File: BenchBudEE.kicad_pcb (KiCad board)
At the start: 4 copper layers, 165.1 x 63.5 mm, 0 parts

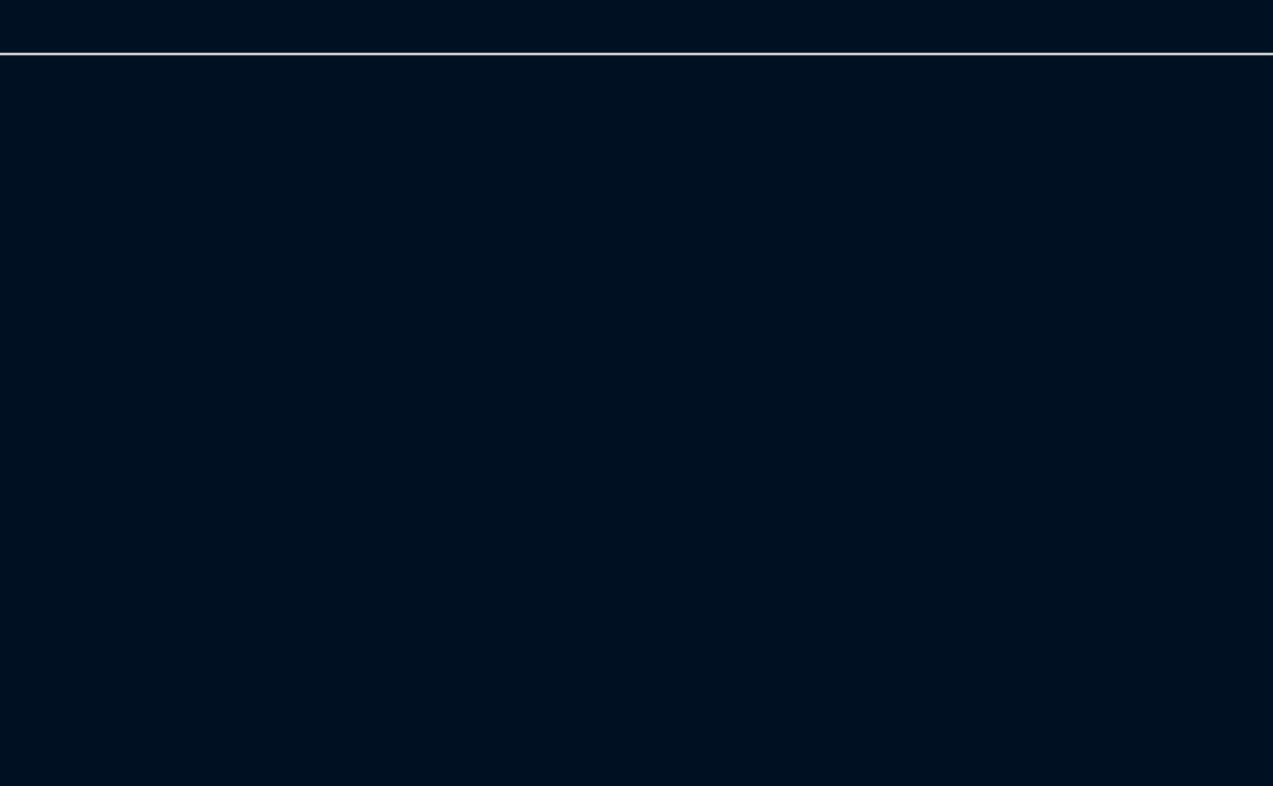
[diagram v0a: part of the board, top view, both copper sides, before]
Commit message: Relay module association and placement
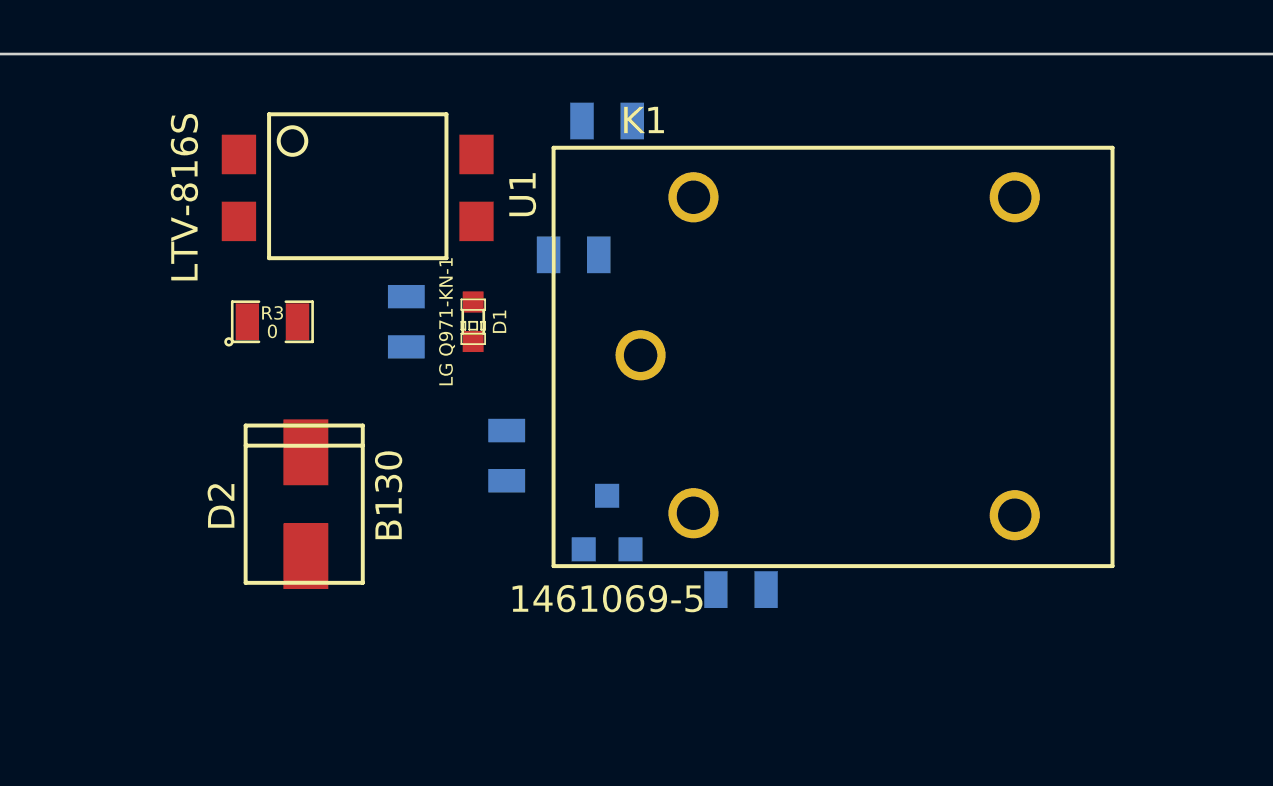
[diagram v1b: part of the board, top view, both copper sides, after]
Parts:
- added D1: LG Q971-KN-1, LED-0603, F.Cu at (251.5, 121.9)
- added D2: B130, SMA, F.Cu at (245.1, 130.8)
- added K1: 1461069-5, TE-SPDT, F.Cu at (257.8, 123.2)
- added Q1: 2N3904, SOT23EBC, B.Cu at (256.5, 129.5)
- added R1: 500, SM0805, B.Cu at (255.3, 119.4)
- added R2: 200, SM0805, B.Cu at (248.9, 121.9)
- added R3: 0, SM0805, F.Cu at (243.8, 121.9)
- added R4: 100, SM0805, B.Cu at (252.7, 127.0)
- added R5: 0, SM0805, B.Cu at (256.5, 114.3)
- added R6: 0, SM0805, B.Cu at (261.6, 132.1)
- added U1: LTV-816S, 4-SMD, F.Cu at (242.6, 115.6)

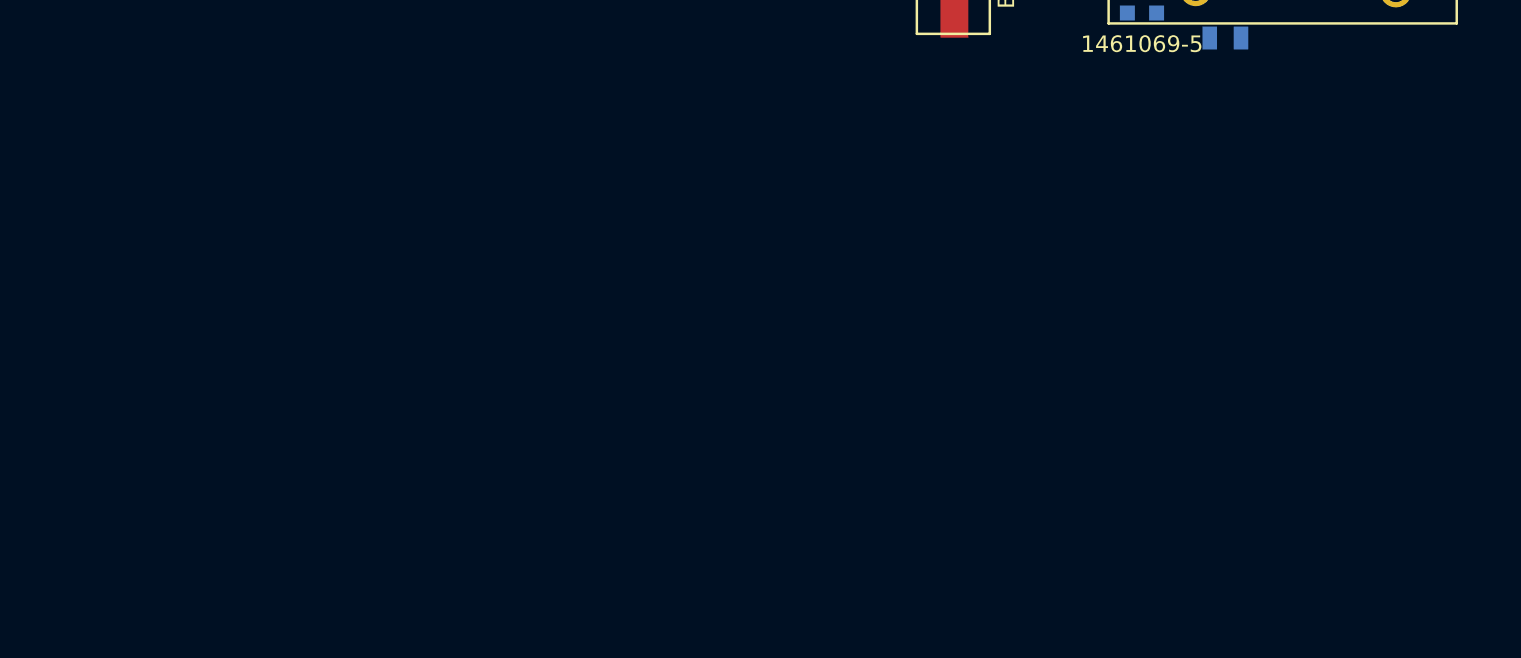
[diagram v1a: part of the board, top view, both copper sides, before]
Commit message: Thermocouple association and placement
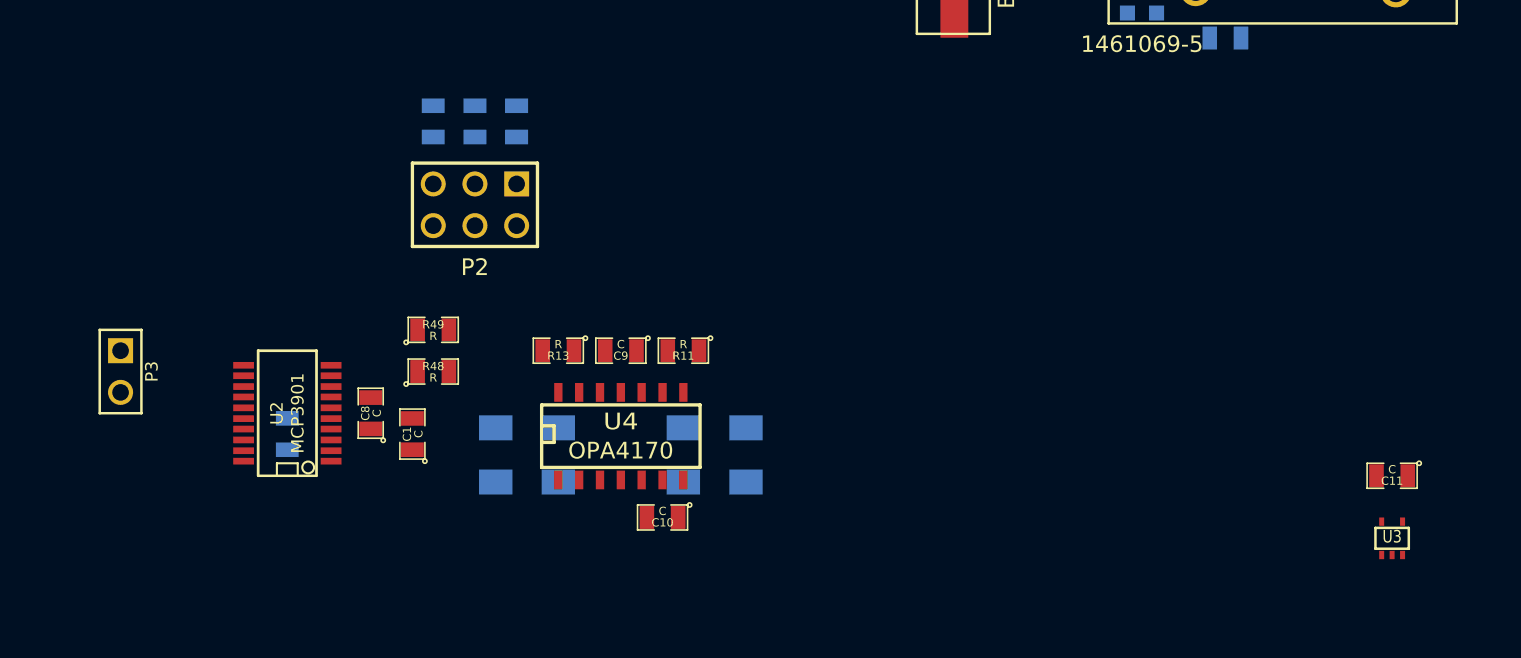
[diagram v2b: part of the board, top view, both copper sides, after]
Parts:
- added C1: C, SM0805, F.Cu at (212.1, 156.2)
- added C10: C, SM0805, F.Cu at (227.3, 161.3)
- added C11: C, SM0805, F.Cu at (271.8, 158.8)
- added C7: C, SM0805, B.Cu at (204.5, 156.2)
- added C8: C, SM0805, F.Cu at (209.6, 154.9)
- added C9: C, SM0805, F.Cu at (224.8, 151.1)
- added P2: CONN_3X2, pin_array_3x2, F.Cu at (215.9, 142.2)
- added P3: CONN_2, PIN_ARRAY_2X1, F.Cu at (194.3, 152.4)
- added R10: R, SM1206, B.Cu at (221.0, 157.5)
- added R11: R, SM0805, F.Cu at (228.6, 151.1)
- added R12: R, SM0805, B.Cu at (215.9, 137.2)
- added R13: R, SM0805, F.Cu at (221.0, 151.1)
- added R44: R, SM0805, B.Cu at (218.4, 137.2)
- added R45: R, SM0805, B.Cu at (213.4, 137.2)
- added R48: R, SM0805, F.Cu at (213.4, 152.4)
- added R49: R, SM0805, F.Cu at (213.4, 149.9)
- added R7: R, SM1206, B.Cu at (217.2, 157.5)
- added R8: R, SM1206, B.Cu at (228.6, 157.5)
- added R9: R, SM1206, B.Cu at (232.4, 157.5)
- added U2: MCP3901, SSOP20, F.Cu at (204.5, 154.9)
- added U3: LMT84, SOT353, F.Cu at (271.8, 162.6)
- added U4: OPA4170, SO14E, F.Cu at (224.8, 156.2)

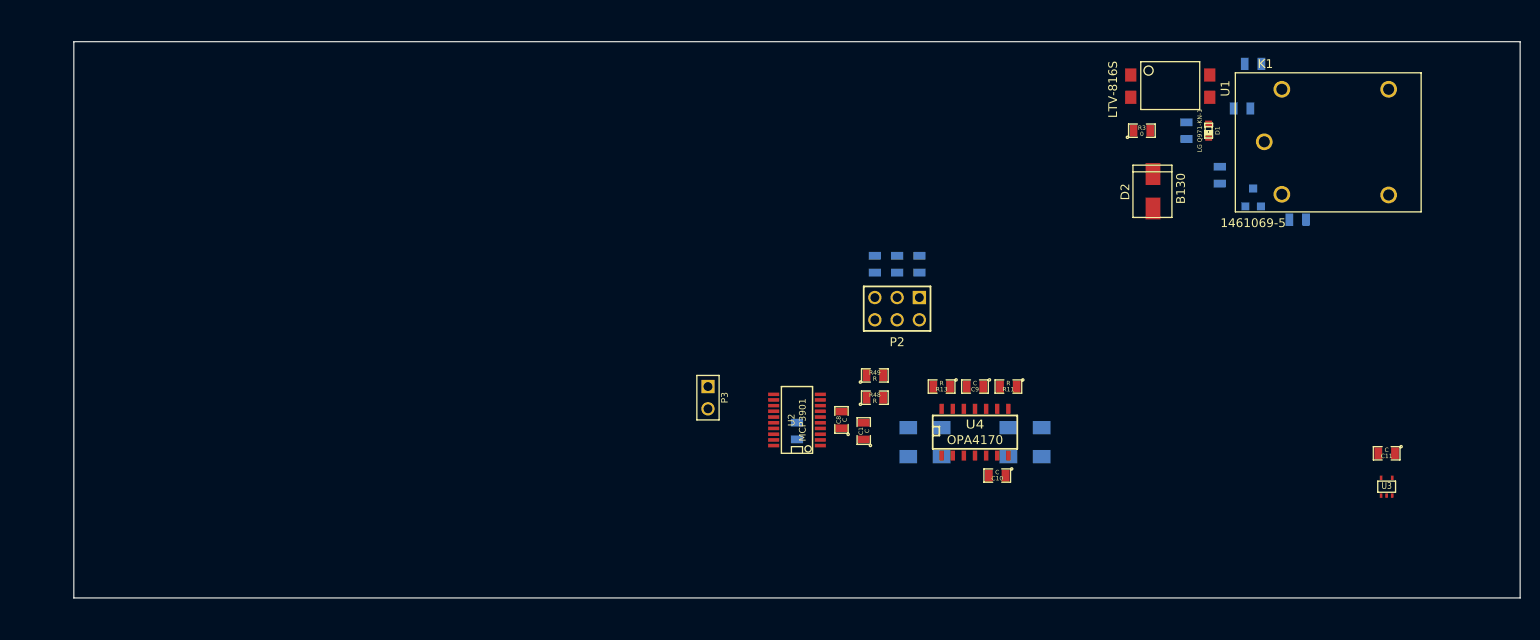
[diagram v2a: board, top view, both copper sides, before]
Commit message: Terminal block and Arduino: assc/placement
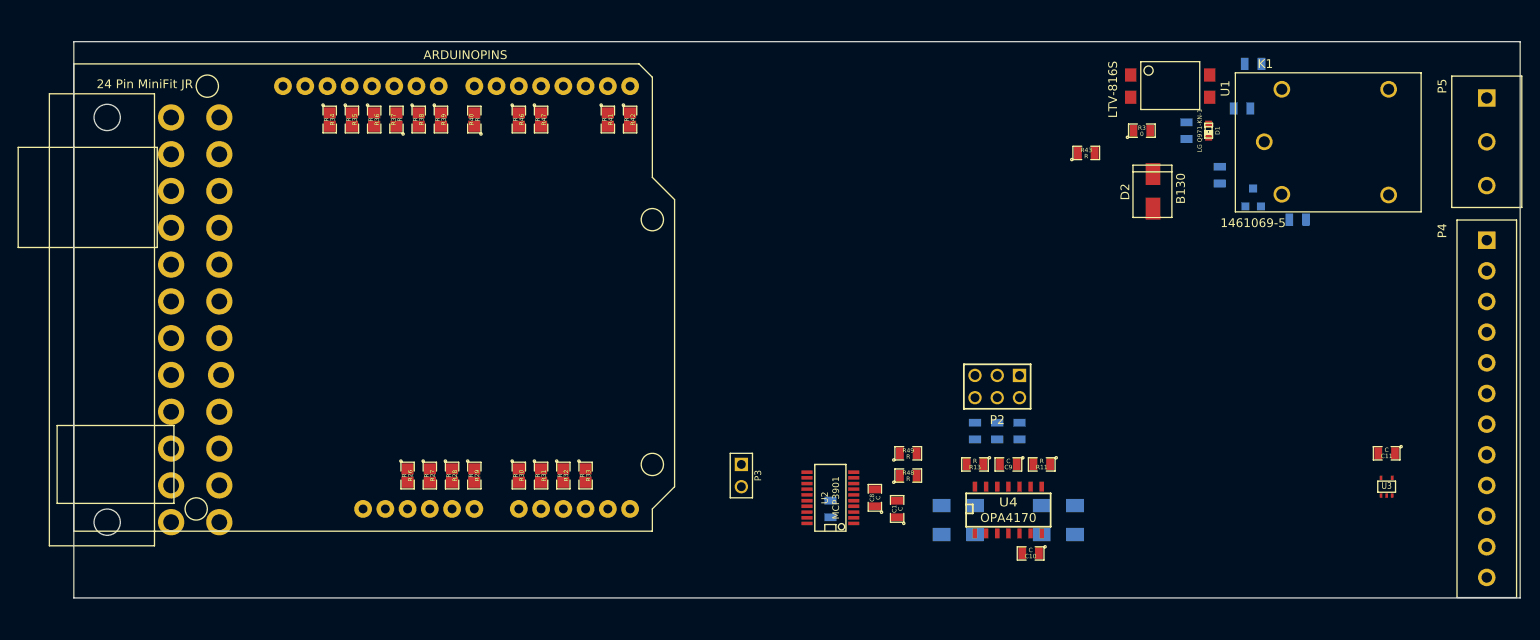
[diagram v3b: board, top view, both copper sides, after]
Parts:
- added ARD1: ARDUINOPINS, Arduino, F.Cu at (121.9, 167.6)
- added P1: 24 Pin MiniFit JR, ATXheader, F.Cu at (125.7, 143.5)
- added P4: 12 Pin Terminal Block, 12pinTB, F.Cu at (283.2, 153.7)
- added P5: 3 Pin TB, 3pinTB, F.Cu at (283.2, 123.2)
- added R26: R, SM0805-blob, F.Cu at (160.0, 161.3)
- added R27: R, SM0805-blob, F.Cu at (162.6, 161.3)
- added R28: R, SM0805-blob, F.Cu at (165.1, 161.3)
- added R29: R, SM0805-blob, F.Cu at (167.6, 161.3)
- added R30: R, SM0805-blob, F.Cu at (172.7, 161.3)
- added R31: R, SM0805-blob, F.Cu at (175.3, 161.3)
- added R32: R, SM0805-blob, F.Cu at (177.8, 161.3)
- added R33: R, SM0805-blob, F.Cu at (180.3, 161.3)
- added R34: R, SM0805-blob, F.Cu at (151.1, 120.7)
- added R35: R, SM0805-blob, F.Cu at (153.7, 120.7)
- added R36: R, SM0805-blob, F.Cu at (156.2, 120.7)
- added R37: R, SM0805-blob, F.Cu at (158.8, 120.7)
- added R38: R, SM0805-blob, F.Cu at (161.3, 120.7)
- added R39: R, SM0805-blob, F.Cu at (163.8, 120.7)
- added R40: R, SM0805-blob, F.Cu at (167.6, 120.7)
- added R41: R, SM0805-blob, F.Cu at (182.9, 120.7)
- added R42: R, SM0805-blob, F.Cu at (185.4, 120.7)
- added R43: R, SM0805, F.Cu at (237.5, 124.5)
- added R46: R, SM0805-blob, F.Cu at (172.7, 120.7)
- added R47: R, SM0805-blob, F.Cu at (175.3, 120.7)
- moved R45 25.2 mm to (229.9, 156.2), turned to 270 degrees
- moved R12 22.2 mm to (227.3, 156.2), turned to 270 degrees
- moved R44 20.1 mm to (224.8, 156.2), turned to 270 degrees
- moved P2 14.5 mm to (227.3, 151.1)
- moved C8 9.67 mm to (213.4, 163.8)
- moved C9 9.67 mm to (228.6, 160.0)
- moved R10 9.67 mm to (224.8, 166.4)
- moved R11 9.67 mm to (232.4, 160.0)
- moved R13 9.67 mm to (224.8, 160.0)
- moved R7 9.67 mm to (221.0, 166.4)
- moved R8 9.67 mm to (232.4, 166.4)
- moved R9 9.67 mm to (236.2, 166.4)
- moved U2 9.67 mm to (208.3, 163.8)
- moved C10 9.67 mm to (231.1, 170.2)
- moved C1 9.67 mm to (215.9, 165.1)
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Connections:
- K1 pad 1: (no net) -> /Relay/RELAY_COM
- K1 pad 3: (no net) -> /Relay/RELAY_NO
- K1 pad 4: (no net) -> /Relay/RELAY_NC
- U4 pad 10: (no net) -> /Thermocouple/TC IN +
- U4 pad 12: (no net) -> /Thermocouple/TC IN -

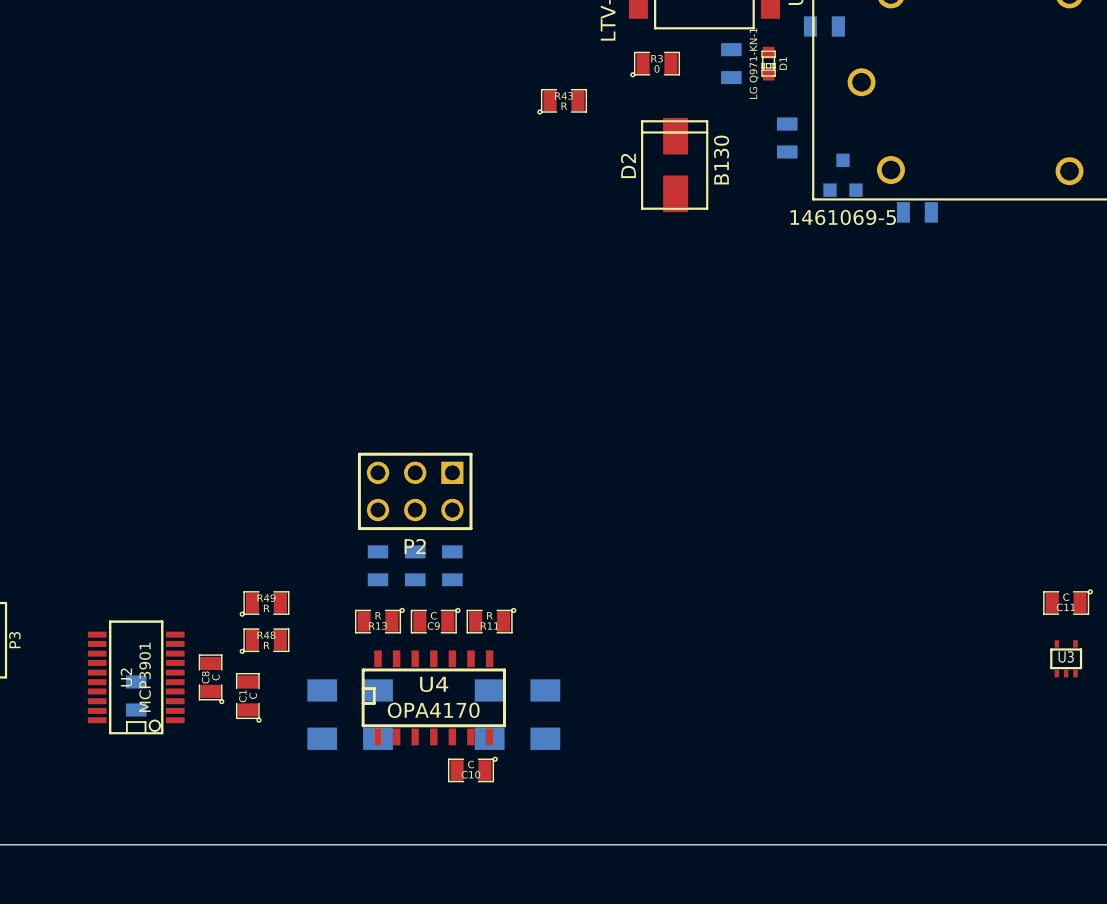
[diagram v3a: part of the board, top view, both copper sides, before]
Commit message: Fan driver: assc/placement
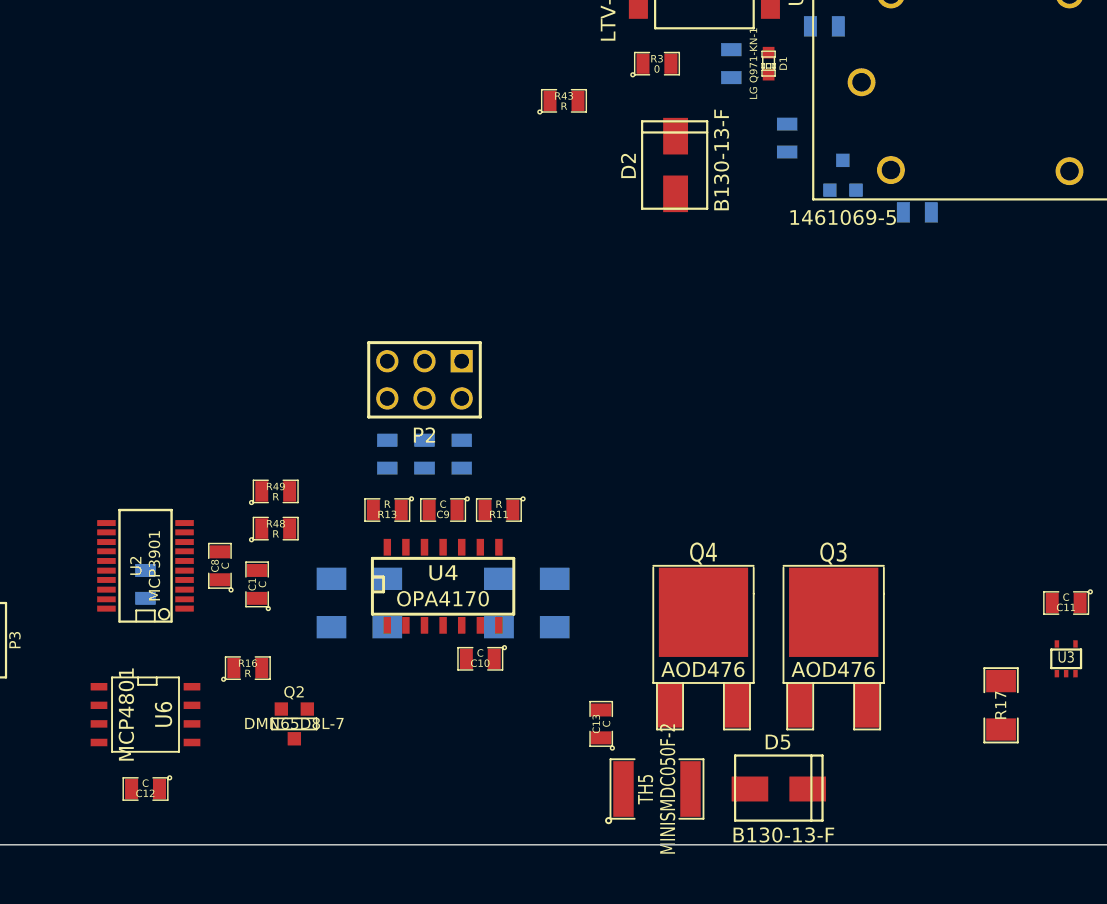
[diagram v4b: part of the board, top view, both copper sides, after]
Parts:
- added C12: C, SM0805, F.Cu at (208.9, 171.4)
- added C13: C, SM0805, F.Cu at (240.0, 167.0)
- added D5: B130-13-F, SMA, F.Cu at (250.2, 171.4)
- added Q2: DMN65D8L-7, SOT23GDS, F.Cu at (219.1, 167.0)
- added Q3: AOD476, DPAK2, F.Cu at (255.9, 165.7)
- added Q4: AOD476, DPAK2, F.Cu at (247.0, 165.7)
- added R16: R, SM0805, F.Cu at (215.9, 163.2)
- added R17: R, SM1206, F.Cu at (267.3, 165.7)
- added TH5: MINISMDC050F-2, SM1812, F.Cu at (243.8, 171.4)
- added U6: MCP4801, SO8N, F.Cu at (208.9, 166.4)
- D2: value B130 -> B130-13-F
- moved C10 7.65 mm to (231.8, 162.6)
- moved C9 7.65 mm to (229.2, 152.4)
- moved R10 7.65 mm to (225.4, 158.8)
- moved R13 7.65 mm to (225.4, 152.4)
- moved R44 7.65 mm to (225.4, 148.6)
- moved R48 7.65 mm to (217.8, 153.7)
- moved R49 7.65 mm to (217.8, 151.1)
- moved R7 7.65 mm to (221.6, 158.8)
- moved U4 7.65 mm to (229.2, 157.5)
- moved C1 7.65 mm to (216.5, 157.5)
- moved C7 7.65 mm to (208.9, 157.5)
- moved C8 7.65 mm to (214.0, 156.2)
- moved P2 7.65 mm to (228.0, 143.5)
- moved R11 7.65 mm to (233.0, 152.4)
- moved R12 7.65 mm to (228.0, 148.6)
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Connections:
- ARD1 pad 13: (no net) -> N-0000052
- ARD1 pad 14: (no net) -> N-0000039
- R39 pad 2: /Arduino/ADC_CS_N -> (no net)
- R40 pad 2: /Fan/CS_N -> (no net)
- U2 pad 17: /Arduino/ADC_CS_N -> (no net)
